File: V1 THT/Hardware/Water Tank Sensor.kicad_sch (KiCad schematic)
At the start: 17 parts, among them J1 Programming port, J2 Temp Sensor, J3 Water Level Sensor, J4 Valve Terminal, J5 12v In, Q1 2N3904, U1 WeMos_D1_mini, U2 LM7805_TO220

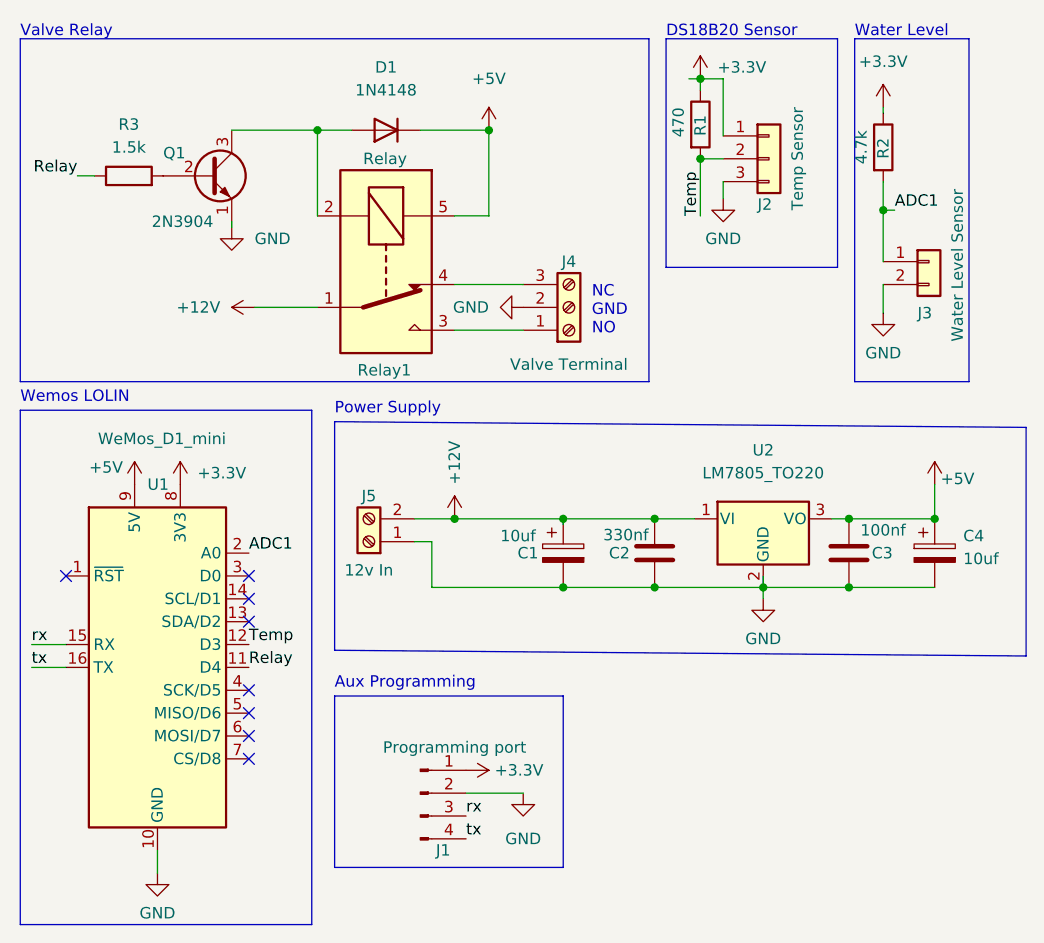
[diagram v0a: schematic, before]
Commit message: Updated files to v1.1 incnluding images annotating resistor to vary depending on ADC sensor.
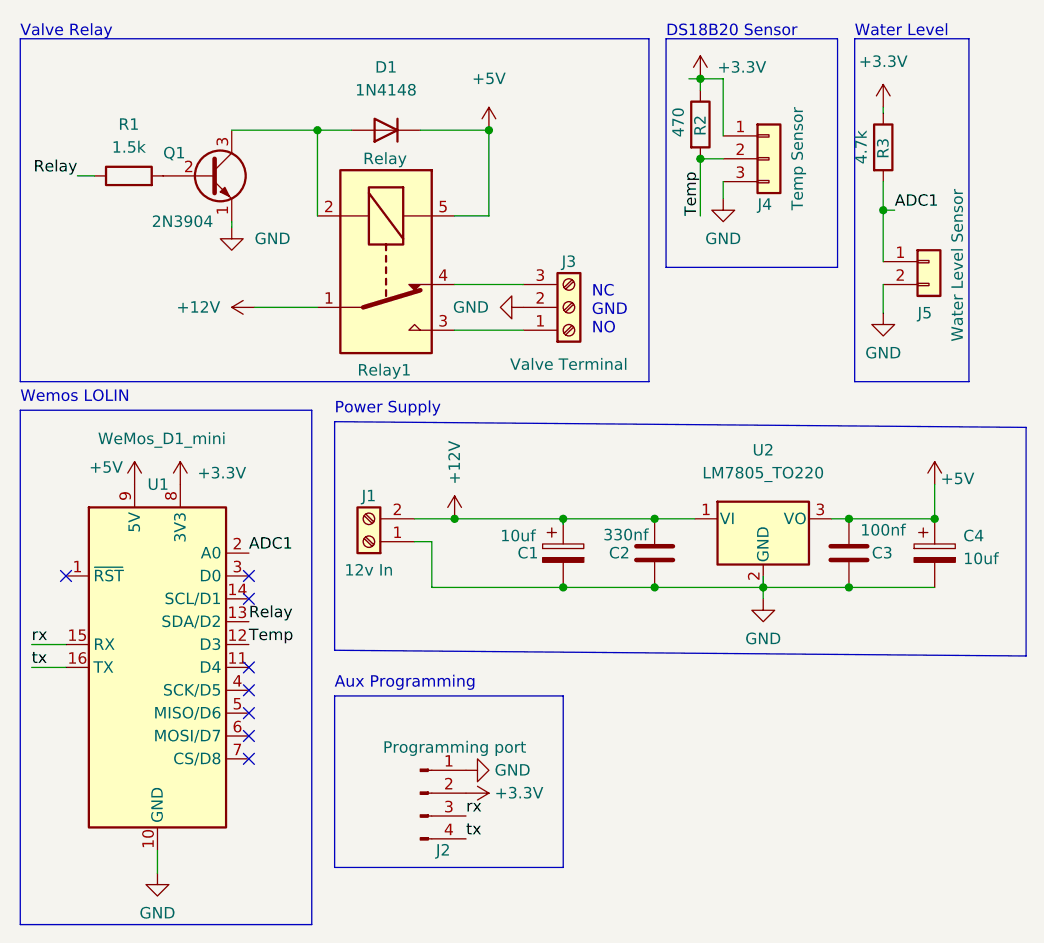
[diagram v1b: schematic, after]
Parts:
- J1: renamed from J5; footprint TerminalBlock:TerminalBlock_bornier-2_P5.08mm -> TerminalBlock_Phoenix:TerminalBlock_Phoenix_MKDS-1,5-2_1x02_P5.00mm_Horizontal
- J2: renamed from J1; footprint Connector_PinHeader_1.27mm:PinHeader_1x04_P1.27mm_Vertical -> Connector_PinSocket_2.54mm:PinSocket_1x04_P2.54mm_Vertical
- J3: renamed from J4; footprint TerminalBlock:TerminalBlock_bornier-3_P5.08mm -> TerminalBlock_Phoenix:TerminalBlock_Phoenix_MKDS-1,5-3_1x03_P5.00mm_Horizontal
- renumbered J2 to J4, J3 to J5, R3 to R1, R1 to R2, R2 to R3
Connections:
- net +3V3: now also J2.2 (Pin_2); no longer J2.1 (Pin_1)
- net GND: now also J2.1 (Pin_1); no longer J2.2 (Pin_2)
- net Relay: now also U1.13 (SDA/D2); no longer U1.11 (D4)

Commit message: Updated v1.2
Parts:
- removed C2: 330nf, Capacitor_THT:C_Disc_D8.0mm_W5.0mm_P5.00mm, symbol Device:C
- removed C3: 100nf, Capacitor_THT:C_Disc_D8.0mm_W5.0mm_P5.00mm, symbol Device:C
- removed U2: LM7805_TO220, Package_TO_SOT_THT:TO-220-3_Vertical, symbol Regulator_Linear:LM7805_TO220
- added D2: Power LED, LED_THT:LED_D3.0mm, symbol Device:LED_Small
- added D3: 1N4148, Diode_THT:D_DO-35_SOD27_P7.62mm_Horizontal, symbol Diode:1N4148
- added D4: Relay, LED_THT:LED_D3.0mm, symbol Device:LED_Small
- added PS1: K7805-500R3, SamacSys_Parts:K7805500R3, symbol SamacSys_Parts:K7805-500R3
- added R4, R5: 10k, Resistor_THT:R_Axial_DIN0207_L6.3mm_D2.5mm_P7.62mm_Horizontal, symbol Device:R_Small
- C4: value 10uf -> 22uf
- J3: renamed from J5; value Water Level Sensor -> Water Level
- J4: renamed from J3; footprint TerminalBlock_Phoenix:TerminalBlock_Phoenix_MKDS-1,5-3_1x03_P5.00mm_Horizontal -> TerminalBlock_Phoenix:TerminalBlock_Phoenix_PT-1,5-3-5.0-H_1x03_P5.00mm_Horizontal
- J5: renamed from J1; footprint TerminalBlock_Phoenix:TerminalBlock_Phoenix_MKDS-1,5-2_1x02_P5.00mm_Horizontal -> TerminalBlock_Phoenix:TerminalBlock_Phoenix_PT-1,5-2-5.0-H_1x02_P5.00mm_Horizontal
- renumbered J2 to J1, J4 to J2, R2 to R1, R3 to R2, R1 to R3
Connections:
- net +12V: now also D3.2 (A); no longer C1.1
- net +5V: now also PS1.3 (VO), R4.1
- net GND: now also D2.1 (K), D4.1 (K), PS1.2 (GND); no longer Q1.1 (E)
- new net: D2.2 (A), R4.2
- new net: D4.2 (A), R5.1
- new net: C1.1, D3.1 (K), PS1.1 (VIN)
- new net: Q1.1 (E), R5.2
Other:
- moved on the sheet: C4, Q1, R3
